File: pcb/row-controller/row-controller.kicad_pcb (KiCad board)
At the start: 2 copper layers, 52.7 x 38.9 mm, 37 parts, among them IC1 INA220BIDGSR, IC2 THVD1420DR, IC3 THVD1420DR, J1 Power In, J2 5555140-2, J3 Power Row, J4 5555140-2, U1 XAIO ESP32-C3, U2 R-78E5.0-0.5

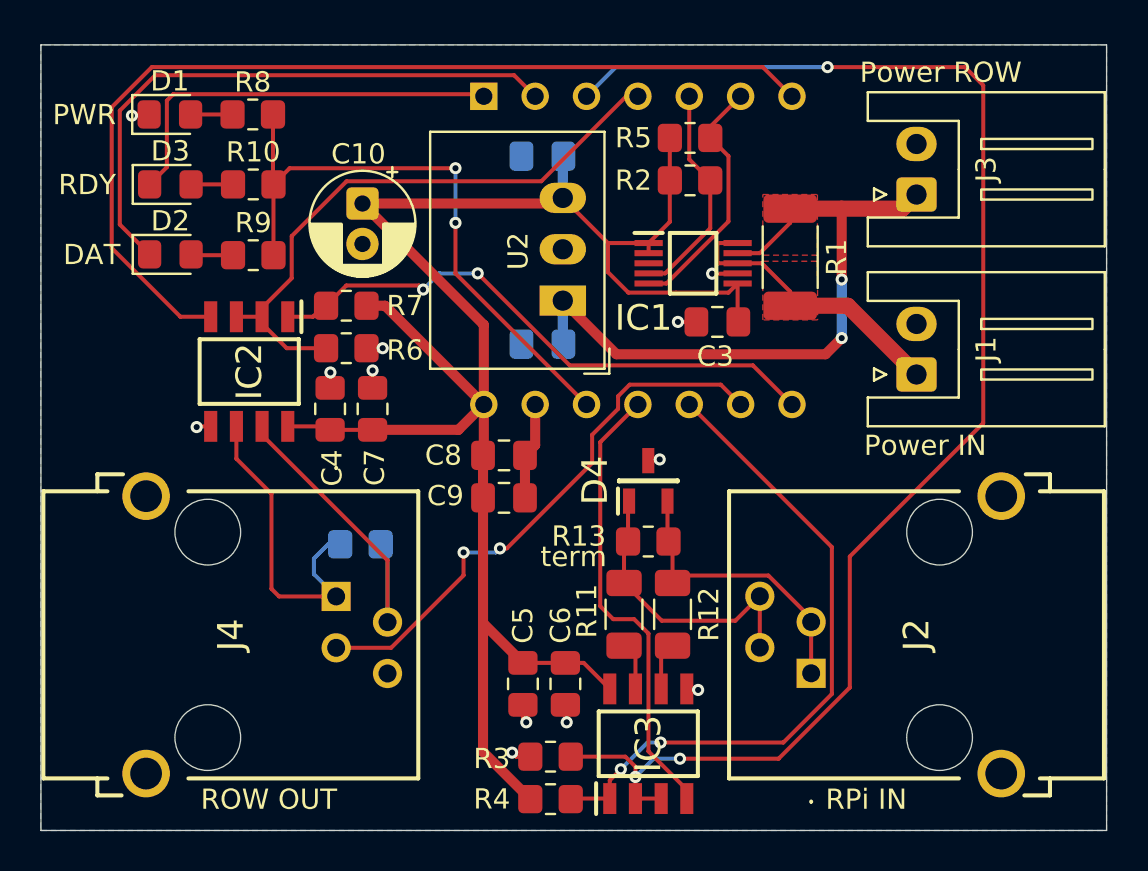
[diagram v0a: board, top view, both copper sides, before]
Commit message: pcb: 3.3V transceiver supply, second Row Bus chain, fab outputs
The THVD1420DR transceivers ran at VCC=5V while driving 3.3V-only GPIOs on
both boards. Per the datasheet the receiver output swings to VCC-0.4V min
(~4.6-4.8V at 5V), and the RX pull-ups went to 5V as well, so both the Pi's
and the RP2350's inputs sat out of spec. Both boards were bodged to 3.3V on
the bench; these schematics bring the sources in line.

pi-hat:
- IC3 supply, decoupling and RX pull-up moved from +5V to +3V3; no +5V net
  remains on the board.
- Second Row Bus chain added (IC4) so the 8 rows split across two chains -
  see docs/row-bus-protocol.md for why one chain no longer fits the frame
  budget. Chain A on uart0 (GPIO14/15), chain B on uart2 (GPIO4/5).
- Both direction lines moved onto the UARTs' own RTS pins, GPIO17 and
  GPIO7, so the kernel's RS-485 mode can eventually drive them with
  hardware timing instead of the host's busy-wait.
- Single RJ45 carries both chains on correctly-paired T568B conductors:
  chain A on pins 1-2, chain B on 3-6, grounds on the blue and brown pairs.

row-controller:
- Both transceivers, the INA220 and its I2C pull-ups moved to +3V3. +5V now
  only feeds the Xiao's VUSB input and the regulator that makes it.
- INA220 VBUS now senses +12V through the 5 mOhm shunt, matching what
  docs/row-bus-protocol.md's POWER command has always claimed it measures;
  it previously sat on the 5V rail and reported ~4.8V.

Also adds v1.0/1.2 gerbers and BOM CSVs, following the existing
gerber-1.1 pattern.

Reviewed the pi-hat netlist in detail - header pins, transceiver
orientation, rails, termination and pairing all check out. The
row-controller and tile changes are carried as-is.

Co-Authored-By: Claude Opus 5 <noreply@anthropic.com>
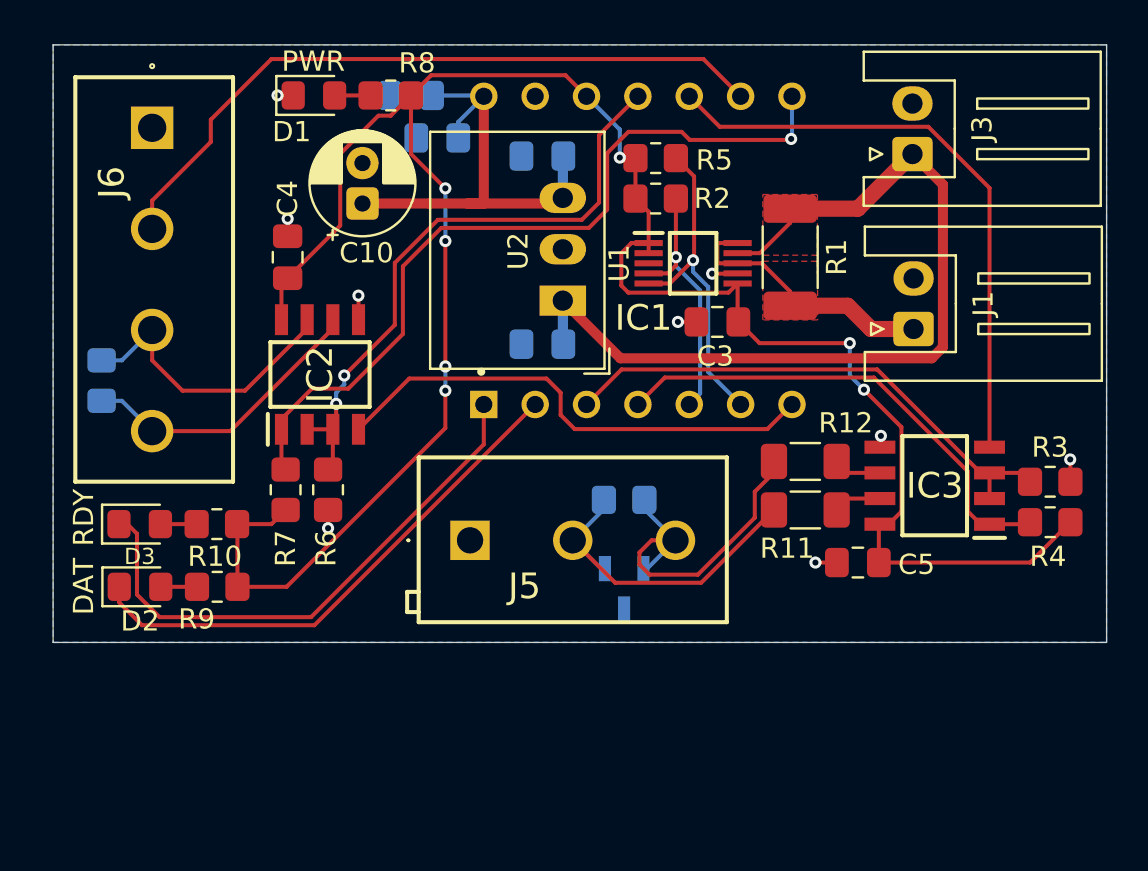
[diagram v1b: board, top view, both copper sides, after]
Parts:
- removed C6, C7: 100nF, Capacitor_SMD:C_0805_2012Metric_Pad1.18x1.45mm_HandSolder
- removed J2, J4: 5555140-2, 5555140-2:55551402
- added J5: Row Bus Header, Garth:1548129, F.Cu at (101.7, 122.3)
- added J6: Tile Bus Header, Garth:TB003-500-P04BE, F.Cu at (86.0, 101.9)
- C3: value .1uF -> 0.1uF
- C4, C5: value 100nF -> 0.1uF
- C8: value .1uF -> 0.1uF; moved to B.Cu
- C9, D4, R13: moved to B.Cu
- R2, R5: value 10K -> 4.7K
- U1: value XAIO ESP32-C3 -> XAIO RP2350; moved to F.Cu
- moved R4 28.3 mm to (130.4, 121.4), turned to 180 degrees
- moved R3 28.2 mm to (130.4, 119.4), turned to 0 degrees
- moved IC3 19.1 mm to (124.7, 119.6), turned to 180 degrees
- moved C8 18.4 mm to (98.8, 100.3), turned to 180 degrees
- moved C9 18.1 mm to (100.1, 102.4), turned to 180 degrees
- moved C5 17.6 mm to (120.9, 123.4), turned to 180 degrees
- moved R10 16.9 mm to (89.2, 121.5)
- moved D3 16.9 mm to (85.4, 121.5)
- moved D2 16.5 mm to (85.4, 124.6)
- moved R9 16.5 mm to (89.2, 124.6)
- moved R14 15.1 mm to (83.5, 114.4), turned to 90 degrees
- moved R11 10.3 mm to (118.3, 120.8), turned to 180 degrees
- moved R12 10.0 mm to (118.3, 118.4), turned to 180 degrees
- moved R7 9.58 mm to (92.6, 119.8), turned to 90 degrees
- moved C4 7.79 mm to (92.7, 108.3)
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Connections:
- net /PI-TRCV-A renamed /PI-TRCV_P
- net /PI-TRCV-B renamed /PI-TRCV_N
- net /ROW-TRCV-A renamed /ROW-TRCV_P
- net /ROW-TRCV-B renamed /ROW-TRCV_N
- C3 pad 2: +5V -> +3V3
- C4 pad 1: +5V -> +3V3
- C5 pad 1: +5V -> +3V3
- IC1 pad 1: +5V -> +3V3
- IC1 pad 2: +5V -> +3V3
- IC1 pad 6: +5V -> +3V3
- IC2 pad 8: +5V -> +3V3
- IC3 pad 8: +5V -> +3V3
- R2 pad 1: +5V -> +3V3
- R4 pad 1: +5V -> +3V3
- R5 pad 1: +5V -> +3V3
- R7 pad 1: +5V -> +3V3
- U1 pad 10: /PI-RxD -> /PI-TxD
- U1 pad 11: /PI-TxD -> /ROW-XDIR
- U1 pad 4: /ROW-XDIR -> /PI-RxD
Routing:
- net +3V3: track 30.7 -> 110.0 mm, vias 2 -> 7
- net +5V: track 92.5 -> 23.8 mm
- net /PI-XDIR: track 71.8 -> 26.2 mm, vias 3 -> 0
- net /ROW-TxD: track 48.3 -> 24.7 mm
- net /ROW-RxD: track 28.7 -> 39.7 mm, vias 2 -> 1
- net Vrow: track 34.2 -> 43.6 mm, vias 2 -> 0
- net /PI-RxD: track 32.8 -> 24.1 mm, vias 2 -> 0
- net /PI-TxD: track 22.6 -> 30.0 mm
- net /ROW-SENSE: track 27.6 -> 34.8 mm, vias 2 -> 0
- net /LED-RDY: track 20.3 -> 27.4 mm
- net GND: track 15.4 -> 8.66 mm, vias 12 -> 9
- net /SCL: track 12.4 -> 16.2 mm, vias 0 -> 1
- net /PI-TRCV_P: track 14.8 -> 18.2 mm
- net /LED-DATA: track 29.4 -> 26.3 mm
- net /PI-TRCV_N: track 14.7 -> 17.1 mm
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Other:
- board size 52.7 x 38.9 mm -> 52.1 x 29.5 mm
- board text added: "2025-10-29 v1.2"
- board text added: "A"
- board text added: "B"
- board text added: "S"
- board text added: "termination"
- board text removed: "2025-10-29 v1.1"
- board text removed: "SENSE"
- board text removed: "TRCV-A"
- board text removed: "TRCV-B"
- board text removed: "term"
